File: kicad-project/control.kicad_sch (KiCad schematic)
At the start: 12 parts, among them SW1 RST_SW, U1 RP2040

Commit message: hw: add RP2040 footprint for hand soldering
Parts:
- U1: footprint AA_PSE_2021:RP2040 -> AA_PPSE_2021:RP2040-Hand-Solder
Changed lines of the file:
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@@
     (property "Reference" "U1" (id 0) (at 132.08 138.43 0))
     (property "Value" "RP2040" (id 1) (at 54.61 38.1 0))
-    (property "Footprint" "AA_PSE_2021:RP2040" (id 2) (at 139.7 60.96 0)
+    (property "Footprint" "AA_PPSE_2021:RP2040-Hand-Solder" (id 2) (at 139.7 60.96 0)
       (effects (font (size 1.27 1.27)) hide)
     )

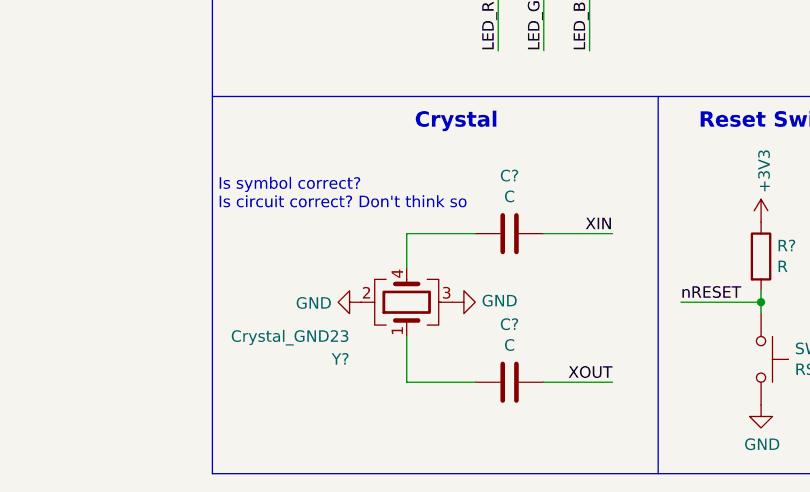
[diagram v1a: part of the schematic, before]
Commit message: hw: fix crystal topology
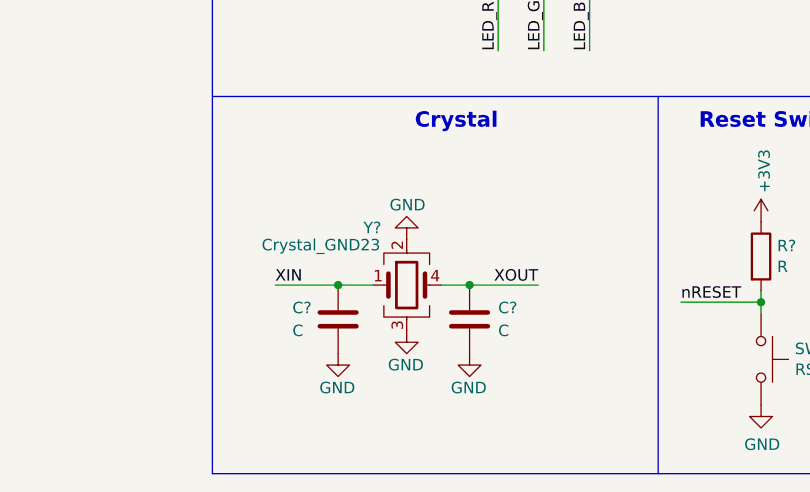
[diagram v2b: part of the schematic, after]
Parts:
- removed C? (x2): C, symbol Device:C
- removed Y?: Crystal_GND23, Crystal:Crystal_SMD_3225-4Pin_3.2x2.5mm, symbol Device:Crystal_GND23
- added C? (x2): C, symbol Device:C
- added Y?: Crystal_GND23, symbol Device:Crystal_GND23
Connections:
- net GND: now also C?.2, C?.2, Y?.2, Y?.3
- net XIN: now also C?.1, Y?.1
- net XOUT: now also C?.1, Y?.4
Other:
- note removed: "Is symbol correct? Is circuit correct? Don't think so"
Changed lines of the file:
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@@
     (company "Thomas Nonis")
   )
+  (junction (at 236.855 141.605) (diameter 0) (color 0 0 0 0)
+  )
   (junction (at 269.24 143.51) (diameter 0) (color 0 0 0 0)
   )
+  (junction (at 222.25 141.605) (diameter 0) (color 0 0 0 0)
+  )
   (junction (at 82.55 31.75) (diameter 0) (color 0 0 0 0)
   )
-  (wire (pts (xy 229.87 152.4) (xy 229.87 147.32))
-    (stroke (width 0) (type default) (color 0 0 0 0))
-  )
   (wire (pts (xy 43.18 85.09) (xy 34.29 85.09))
     (stroke (width 0) (type default) (color 0 0 0 0))
   )
-  (wire (pts (xy 237.49 152.4) (xy 229.87 152.4))
-    (stroke (width 0) (type default) (color 0 0 0 0))
-  )
   (wire (pts (xy 80.01 31.75) (xy 82.55 31.75))
     (stroke (width 0) (type default) (color 0 0 0 0))
@@
     (stroke (width 0) (type default) (color 0 0 0 0))
   )
-  (wire (pts (xy 229.87 135.89) (xy 237.49 135.89))
-    (stroke (width 0) (type default) (color 0 0 0 0))
-  )
   (wire (pts (xy 43.18 119.38) (xy 30.48 119.38))
     (stroke (width 0) (type default) (color 0 0 0 0))
@@
     (stroke (width 0) (type default) (color 0 0 0 0))
   )
+  (wire (pts (xy 233.68 141.605) (xy 236.855 141.605))
+    (stroke (width 0) (type default) (color 0 0 0 0))
+  )
   (polyline (pts (xy 208.28 78.74) (xy 208.28 162.56))
     (stroke (width 0) (type default) (color 0 0 0 0))
@@
     (stroke (width 0) (type default) (color 0 0 0 0))
   )
-  (wire (pts (xy 245.11 135.89) (xy 252.73 135.89))
-    (stroke (width 0) (type default) (color 0 0 0 0))
-  )
-  (wire (pts (xy 245.11 152.4) (xy 252.73 152.4))
+  (wire (pts (xy 215.265 141.605) (xy 222.25 141.605))
+    (stroke (width 0) (type default) (color 0 0 0 0))
+  )
+  (wire (pts (xy 236.855 141.605) (xy 244.475 141.605))
     (stroke (width 0) (type default) (color 0 0 0 0))
   )
@@
     (stroke (width 0) (type default) (color 0 0 0 0))
   )
-  (wire (pts (xy 229.87 139.7) (xy 229.87 135.89))
+  (wire (pts (xy 222.25 141.605) (xy 226.06 141.605))
     (stroke (width 0) (type default) (color 0 0 0 0))
   )
@@
     (effects (font (size 1.27 1.27)) (justify left bottom))
   )
-  (text "Is symbol correct?\nIs circuit correct? Don't think so"
-    (at 208.915 133.35 0)
-    (effects (font (size 1.27 1.27)) (justify left bottom))
-  )
   (text "RGB LED" (at 251.46 82.55 180)
     (effects (font (size 1.7018 1.7018) (thickness 0.3404) bold) (justify right bottom))
@@
     (effects (font (size 1.27 1.27)) (justify left bottom))
   )
-  (label "XOUT" (at 252.73 152.4 180)
+  (label "XOUT" (at 244.475 141.605 180)
     (effects (font (size 1.27 1.27)) (justify right bottom))
   )
@@
     (effects (font (size 1.27 1.27)) (justify left bottom))
   )
+  (label "XIN" (at 215.265 141.605 0)
+    (effects (font (size 1.27 1.27)) (justify left bottom))
+  )
   (label "XIN" (at 34.29 85.09 0)
     (effects (font (size 1.27 1.27)) (justify left bottom))
@@
   (label "LED_B" (at 250.19 115.57 90)
     (effects (font (size 1.27 1.27)) (justify left bottom))
-  )
-  (label "XIN" (at 252.73 135.89 180)
-    (effects (font (size 1.27 1.27)) (justify right bottom))
   )
   (label "FLASH_CLK" (at 30.48 114.3 0)
@@
     (pin "1")
   )
-  (symbol (lib_id "Device:Crystal_GND23") (at 229.87 143.51 90) (unit 1)
-    (in_bom yes) (on_board yes)
-    (property "Reference" "Y?" (id 0) (at 223.52 149.86 90)
-      (effects (font (size 1.27 1.27)) (justify left))
-    )
-    (property "Value" "Crystal_GND23" (id 1) (at 223.52 147.32 90)
-      (effects (font (size 1.27 1.27)) (justify left))
-    )
-    (property "Footprint" "Crystal:Crystal_SMD_3225-4Pin_3.2x2.5mm" (id 2) (at 229.87 143.51 0)
-      (effects (font (size 1.27 1.27)) hide)
-    )
-    (property "Datasheet" "~" (id 3) (at 229.87 143.51 0)
-      (effects (font (size 1.27 1.27)) hide)
-    )
-    (pin "1")
-    (pin "2")
-    (pin "3")
-    (pin "4")
-  )
-  (symbol (lib_id "Device:C") (at 241.3 152.4 270) (unit 1)
-    (in_bom yes) (on_board yes)
-    (property "Reference" "C?" (id 0) (at 241.3 145.9992 90))
-    (property "Value" "C" (id 1) (at 241.3 148.3106 90))
-    (property "Footprint" "" (id 2) (at 237.49 153.3652 0)
-      (effects (font (size 1.27 1.27)) hide)
-    )
-    (property "Datasheet" "~" (id 3) (at 241.3 152.4 0)
-      (effects (font (size 1.27 1.27)) hide)
-    )
-    (pin "1")
-    (pin "2")
-  )
-  (symbol (lib_id "Device:C") (at 241.3 135.89 270) (unit 1)
-    (in_bom yes) (on_board yes)
-    (property "Reference" "C?" (id 0) (at 241.3 129.4892 90))
-    (property "Value" "C" (id 1) (at 241.3 131.8006 90))
-    (property "Footprint" "" (id 2) (at 237.49 136.8552 0)
-      (effects (font (size 1.27 1.27)) hide)
-    )
-    (property "Datasheet" "~" (id 3) (at 241.3 135.89 0)
-      (effects (font (size 1.27 1.27)) hide)
-    )
-    (pin "1")
-    (pin "2")
-  )
-  (symbol (lib_id "power:GND") (at 224.79 143.51 270) (unit 1)
-    (in_bom yes) (on_board yes)
-    (property "Reference" "#PWR?" (id 0) (at 218.44 143.51 0)
-      (effects (font (size 1.27 1.27)) hide)
-    )
-    (property "Value" "GND" (id 1) (at 221.5388 143.637 90)
+  (symbol (lib_id "power:GND") (at 229.87 146.685 0) (unit 1)
+    (in_bom yes) (on_board yes)
+    (property "Reference" "#PWR?" (id 0) (at 229.87 153.035 0)
+      (effects (font (size 1.27 1.27)) hide)
+    )
+    (property "Value" "GND" (id 1) (at 231.775 150.495 0)
       (effects (font (size 1.27 1.27)) (justify right))
     )
-    (property "Footprint" "" (id 2) (at 224.79 143.51 0)
-      (effects (font (size 1.27 1.27)) hide)
-    )
-    (property "Datasheet" "" (id 3) (at 224.79 143.51 0)
-      (effects (font (size 1.27 1.27)) hide)
-    )
-    (pin "1")
-  )
-  (symbol (lib_id "power:GND") (at 234.95 143.51 90) (unit 1)
-    (in_bom yes) (on_board yes)
-    (property "Reference" "#PWR?" (id 0) (at 241.3 143.51 0)
-      (effects (font (size 1.27 1.27)) hide)
-    )
-    (property "Value" "GND" (id 1) (at 238.2012 143.383 90)
+    (property "Footprint" "" (id 2) (at 229.87 146.685 0)
+      (effects (font (size 1.27 1.27)) hide)
+    )
+    (property "Datasheet" "" (id 3) (at 229.87 146.685 0)
+      (effects (font (size 1.27 1.27)) hide)
+    )
+    (pin "1")
+  )
+  (symbol (lib_id "power:GND") (at 229.87 136.525 180) (unit 1)
+    (in_bom yes) (on_board yes)
+    (property "Reference" "#PWR?" (id 0) (at 229.87 130.175 0)
+      (effects (font (size 1.27 1.27)) hide)
+    )
+    (property "Value" "GND" (id 1) (at 227.965 132.715 0)
       (effects (font (size 1.27 1.27)) (justify right))
     )
-    (property "Footprint" "" (id 2) (at 234.95 143.51 0)
-      (effects (font (size 1.27 1.27)) hide)
-    )
-    (property "Datasheet" "" (id 3) (at 234.95 143.51 0)
+    (property "Footprint" "" (id 2) (at 229.87 136.525 0)
+      (effects (font (size 1.27 1.27)) hide)
+    )
+    (property "Datasheet" "" (id 3) (at 229.87 136.525 0)
       (effects (font (size 1.27 1.27)) hide)
     )
@@
       (effects (font (size 1.27 1.27)) hide)
     )
+    (pin "1")
+  )
+  (symbol (lib_id "Device:C") (at 222.25 145.415 0) (unit 1)
+    (in_bom yes) (on_board yes)
+    (property "Reference" "C?" (id 0) (at 217.17 144.145 0)
+      (effects (font (size 1.27 1.27)) (justify left))
+    )
+    (property "Value" "C" (id 1) (at 217.17 146.685 0)
+      (effects (font (size 1.27 1.27)) (justify left))
+    )
+    (property "Footprint" "" (id 2) (at 223.2152 149.225 0)
+      (effects (font (size 1.27 1.27)) hide)
+    )
+    (property "Datasheet" "~" (id 3) (at 222.25 145.415 0)
+      (effects (font (size 1.27 1.27)) hide)
+    )
+    (pin "1")
+    (pin "2")
+  )
+  (symbol (lib_id "Device:C") (at 236.855 145.415 0) (unit 1)
+    (in_bom yes) (on_board yes) (fields_autoplaced)
+    (property "Reference" "C?" (id 0) (at 240.03 144.1449 0)
+      (effects (font (size 1.27 1.27)) (justify left))
+    )
+    (property "Value" "C" (id 1) (at 240.03 146.6849 0)
+      (effects (font (size 1.27 1.27)) (justify left))
+    )
+    (property "Footprint" "" (id 2) (at 237.8202 149.225 0)
+      (effects (font (size 1.27 1.27)) hide)
+    )
+    (property "Datasheet" "~" (id 3) (at 236.855 145.415 0)
+      (effects (font (size 1.27 1.27)) hide)
+    )
+    (pin "1")
+    (pin "2")
+  )
+  (symbol (lib_id "Device:Crystal_GND23") (at 229.87 141.605 0) (unit 1)
+    (in_bom yes) (on_board yes)
+    (property "Reference" "Y?" (id 0) (at 226.06 135.255 0))
+    (property "Value" "Crystal_GND23" (id 1) (at 220.345 137.16 0))
+    (property "Footprint" "" (id 2) (at 229.87 141.605 0)
+      (effects (font (size 1.27 1.27)) hide)
+    )
+    (property "Datasheet" "~" (id 3) (at 229.87 141.605 0)
+      (effects (font (size 1.27 1.27)) hide)
+    )
+    (pin "1")
+    (pin "2")
+    (pin "3")
+    (pin "4")
+  )
+  (symbol (lib_id "power:GND") (at 222.25 149.225 0) (unit 1)
+    (in_bom yes) (on_board yes)
+    (property "Reference" "#PWR?" (id 0) (at 222.25 155.575 0)
+      (effects (font (size 1.27 1.27)) hide)
+    )
+    (property "Value" "GND" (id 1) (at 224.155 153.035 0)
+      (effects (font (size 1.27 1.27)) (justify right))
+    )
+    (property "Footprint" "" (id 2) (at 222.25 149.225 0)
+      (effects (font (size 1.27 1.27)) hide)
+    )
+    (property "Datasheet" "" (id 3) (at 222.25 149.225 0)
+      (effects (font (size 1.27 1.27)) hide)
+    )
+    (pin "1")
+  )
+  (symbol (lib_id "power:GND") (at 236.855 149.225 0) (unit 1)
+    (in_bom yes) (on_board yes)
+    (property "Reference" "#PWR?" (id 0) (at 236.855 155.575 0)
+      (effects (font (size 1.27 1.27)) hide)
+    )
+    (property "Value" "GND" (id 1) (at 238.76 153.035 0)
+      (effects (font (size 1.27 1.27)) (justify right))
+    )
+    (property "Footprint" "" (id 2) (at 236.855 149.225 0)
+      (effects (font (size 1.27 1.27)) hide)
+    )
+    (property "Datasheet" "" (id 3) (at 236.855 149.225 0)
+      (effects (font (size 1.27 1.27)) hide)
+    )

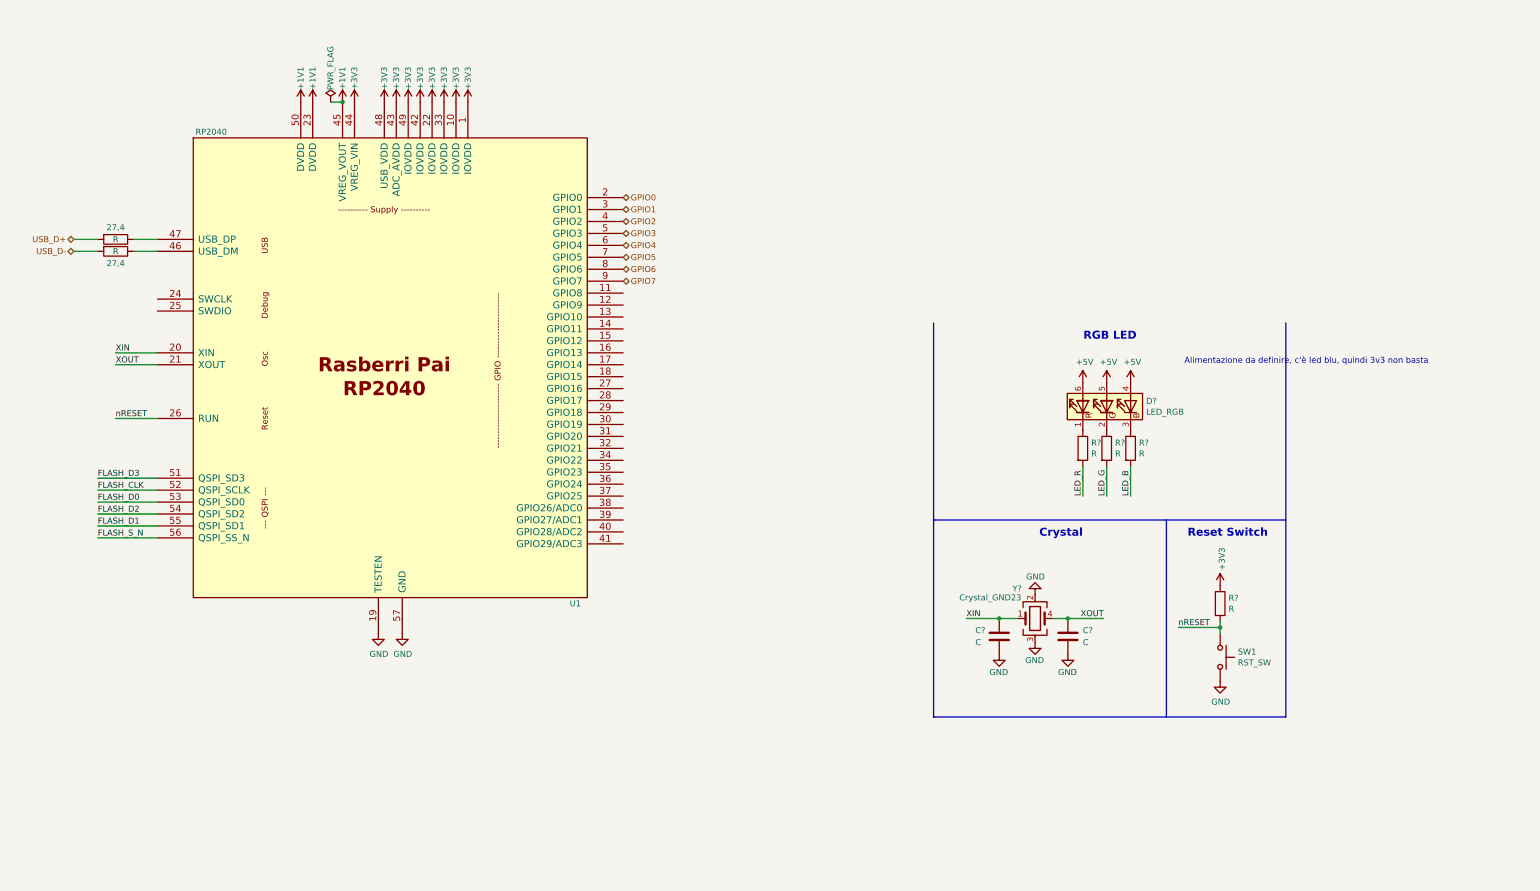
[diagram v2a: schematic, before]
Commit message: hw: add flash, switching circuit and XOUT resistor, change GPS and general cleanup
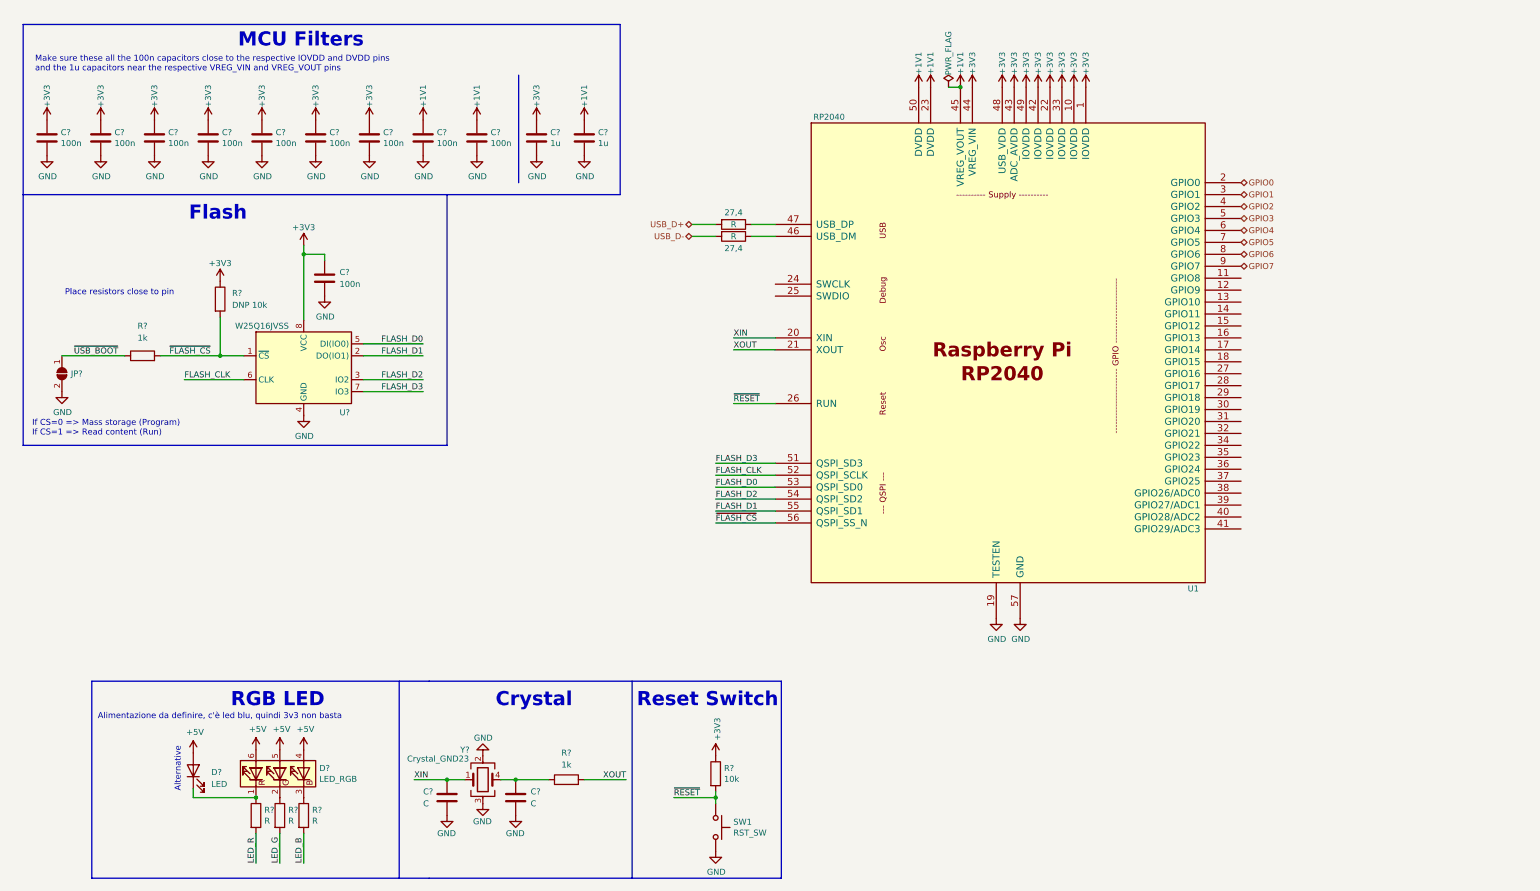
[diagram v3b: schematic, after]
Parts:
- added C? (x9): 100n, Capacitor_SMD:C_0603_1608Metric, symbol Device:C
- added C?: 100n, symbol Device:C
- added C? (x2): 1u, Capacitor_SMD:C_0603_1608Metric, symbol Device:C
- added D?: LED, symbol Device:LED
- added JP?: SolderJumper_2_Open, symbol Jumper:SolderJumper_2_Open
- added R? (x2): 1k, symbol Device:R
- added R?: DNP 10k, symbol Device:R
- added U?: W25Q16JVSS, Package_SO:SOIC-8_5.23x5.23mm_P1.27mm, symbol Memory_Flash:W25Q32JVSS
- R?: value R -> 10k
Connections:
- net +1V1: now also C?.1, C?.1, C?.1
- net +3V3: now also C?.1, C?.1, C?.1, C?.1, C?.1, C?.1, C?.1, C?.1, C?.1, R?.1, U?.8 (VCC)
- net +5V: now also D?.2 (A)
- net FLASH_CLK: now also U?.6 (CLK)
- net FLASH_D0: now also U?.5 (DI(IO0))
- net FLASH_D1: now also U?.2 (DO(IO1))
- net FLASH_D2: now also U?.3 (IO2)
- net FLASH_D3: now also U?.7 (IO3)
- net GND: now also C?.2, C?.2, C?.2, C?.2, C?.2, C?.2, C?.2, C?.2, C?.2, C?.2, C?.2, C?.2, JP?.2 (B), U?.4 (GND)
- net XOUT: now also R?.2; no longer C?.1, Y?.4
- net at D?.1 (RK), R?.1: now also D?.1 (K)
- net FLASH_S_N renamed ~{FLASH_CS}
- net ~{FLASH_CS}: now also R?.2, R?.2, U?.1 (~{CS})
- net nRESET renamed ~{RESET}
- new net: C?.1, R?.1, Y?.4
- new net ~{USB_BOOT}: JP?.1 (A), R?.1
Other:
- note added: "Alternative"
- note added: "Flash"
- note added: "If CS=0 => Mass storage (Program) If CS=1 => Read content (Run)"
- note added: "MCU Filters"
- note added: "Make sure these all the 100n capacitors close to the respective IOVDD and DVDD pins and the 1u capacitors near the respective VREG_VIN and VREG_VOUT pins"
- note added: "Place resistors close to pin"
- moved on the sheet: 27,4, C?, D?, R?, SW1, U1, Y?
